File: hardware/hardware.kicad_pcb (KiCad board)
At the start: 2 copper layers, 33 x 44.4 mm, 18 parts, among them P1 PROG. UART, P2 WS2811, U1 MCP1754ST-3302E/MB, U2 74LS123, U3 SN74LV1T34

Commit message: Insert final timing component values and fix a missing trace in PCB.
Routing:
- net +3V3: track 66.3 -> 80.0 mm
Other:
- board text added: "SUBSPACE SIGN LED CONTROLLER R2 © 2016 MAKERS-IE"
- board text removed: "SUBSPACE SIGN LED CONTROLLER R1 © 2016 MAKERS-IE"
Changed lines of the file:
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@@
   (general
     (links 48)
-    (no_connects 1)
+    (no_connects 0)
     (area 69.992572 22.779999 132.445429 80.090001)
     (thickness 1.6)
     (drawings 11)
-    (tracks 176)
+    (tracks 179)
     (zones 0)
     (modules 18)
@@
     (32 B.Adhes user)
     (33 F.Adhes user)
-    (34 B.Paste user)
+    (34 B.Paste user hide)
     (35 F.Paste user)
-    (36 B.SilkS user hide)
+    (36 B.SilkS user)
     (37 F.SilkS user hide)
     (38 B.Mask user)
@@
   )
   (setup
-    (last_trace_width 0.5)
+    (last_trace_width 0.375)
     (user_trace_width 0.375)
     (trace_clearance 0.2)
@@
       (effects (font (size 1 1) (thickness 0.15)))
     )
-    (fp_text value "PROG. UART" (at -2.667 6.35 360) (layer F.SilkS)
+    (fp_text value "PROG. UART" (at 3.175 19.304 360) (layer F.SilkS)
       (effects (font (size 1 1) (thickness 0.15)))
     )
@@
   (gr_line (start 78.74 77.47) (end 127 77.47) (angle 90) (layer Eco1.User) (width 0.15))
   (gr_line (start 78.74 29.21) (end 78.74 77.47) (angle 90) (layer Eco1.User) (width 0.15))
-  (gr_text "SUBSPACE SIGN\nLED CONTROLLER R1\n© 2016 MAKERS-IE" (at 93.472 39.624) (layer B.SilkS)
+  (gr_text "SUBSPACE SIGN\nLED CONTROLLER R2\n© 2016 MAKERS-IE" (at 93.472 39.624) (layer B.SilkS)
     (effects (font (size 1.5 1.5) (thickness 0.3)) (justify mirror))
   )
@@
   (segment (start 83.82 46.228) (end 86.868 46.228) (width 0.5) (layer F.Cu) (net 2))
   (segment (start 81.788 44.196) (end 83.82 46.228) (width 0.5) (layer F.Cu) (net 2))
+  (segment (start 92.456 56.007) (end 93.853 57.404) (width 0.5) (layer F.Cu) (net 3))
+  (segment (start 104.394 57.404) (end 105.25 58.26) (width 0.5) (layer F.Cu) (net 3))
+  (segment (start 93.853 57.404) (end 104.394 57.404) (width 0.5) (layer F.Cu) (net 3))
   (segment (start 106.426 45.72) (end 107.25 46.544) (width 0.5) (layer F.Cu) (net 3))
   (segment (start 107.25 46.544) (end 107.25 47.844) (width 0.5) (layer F.Cu) (net 3))
@@
   (segment (start 105.25 62.86502) (end 105.25 59.944) (width 0.5) (layer F.Cu) (net 3) (status 30))
   (segment (start 107.25 47.844) (end 107.25 49.214) (width 0.5) (layer F.Cu) (net 3) (status 10))
+  (segment (start 105.25 56.896) (end 105.25 58.26) (width 0.5) (layer F.Cu) (net 3) (status 20))
+  (segment (start 105.25 51.214) (end 105.25 56.896) (width 0.5) (layer F.Cu) (net 3))
   (segment (start 107.25 49.214) (end 105.25 51.214) (width 0.5) (layer F.Cu) (net 3))
-  (segment (start 105.25 51.214) (end 105.25 56.896) (width 0.5) (layer F.Cu) (net 3))
-  (segment (start 105.25 56.896) (end 105.25 59.944) (width 0.5) (layer F.Cu) (net 3) (status 20))
+  (segment (start 105.25 58.26) (end 105.25 59.944) (width 0.5) (layer F.Cu) (net 3) (status 20))
   (segment (start 87.376 40.706) (end 88.031 41.361) (width 0.375) (layer F.Cu) (net 4))
   (segment (start 88.031 41.361) (end 90.014 41.361) (width 0.375) (layer F.Cu) (net 4))
@@
   (segment (start 99.06 43.18) (end 99.06 44.45) (width 0.375) (layer F.Cu) (net 17))
   (segment (start 97.241 41.361) (end 99.06 43.18) (width 0.375) (layer F.Cu) (net 17))
-  (segment (start 95.25 55.88) (end 95.25 56.896) (width 0.5) (layer F.Cu) (net 19))
-  (segment (start 95.25 56.896) (end 95.25 56.992) (width 0.5) (layer B.Cu) (net 19))
-  (via (at 95.25 56.896) (size 0.6) (drill 0.4) (layers F.Cu B.Cu) (net 19))
-  (segment (start 94.838 57.404) (end 95.25 56.992) (width 0.5) (layer B.Cu) (net 19))
-  (segment (start 94.838 61.976) (end 94.838 57.404) (width 0.5) (layer B.Cu) (net 19) (status 10))
+  (segment (start 95.25 47.844) (end 95.25 56.388) (width 0.5) (layer F.Cu) (net 19))
+  (segment (start 94.838 56.8) (end 94.838 61.976) (width 0.5) (layer B.Cu) (net 19))
+  (segment (start 94.996 56.642) (end 94.838 56.8) (width 0.5) (layer B.Cu) (net 19))
+  (via (at 94.996 56.642) (size 0.6) (drill 0.4) (layers F.Cu B.Cu) (net 19))
+  (segment (start 95.25 56.388) (end 94.996 56.642) (width 0.5) (layer F.Cu) (net 19))
   (segment (start 105.41 69.215) (end 105.41 66.675) (width 0.5) (layer F.Cu) (net 19) (status 10))
   (segment (start 105.41 66.675) (end 104.013 65.278) (width 0.5) (layer F.Cu) (net 19))
-  (segment (start 95.25 55.88) (end 95.25 47.844) (width 0.5) (layer F.Cu) (net 19) (status 20))
   (segment (start 94.838 64.612) (end 94.838 61.976) (width 0.5) (layer B.Cu) (net 19) (status 20))
   (segment (start 94.996 64.77) (end 94.838 64.612) (width 0.5) (layer B.Cu) (net 19))

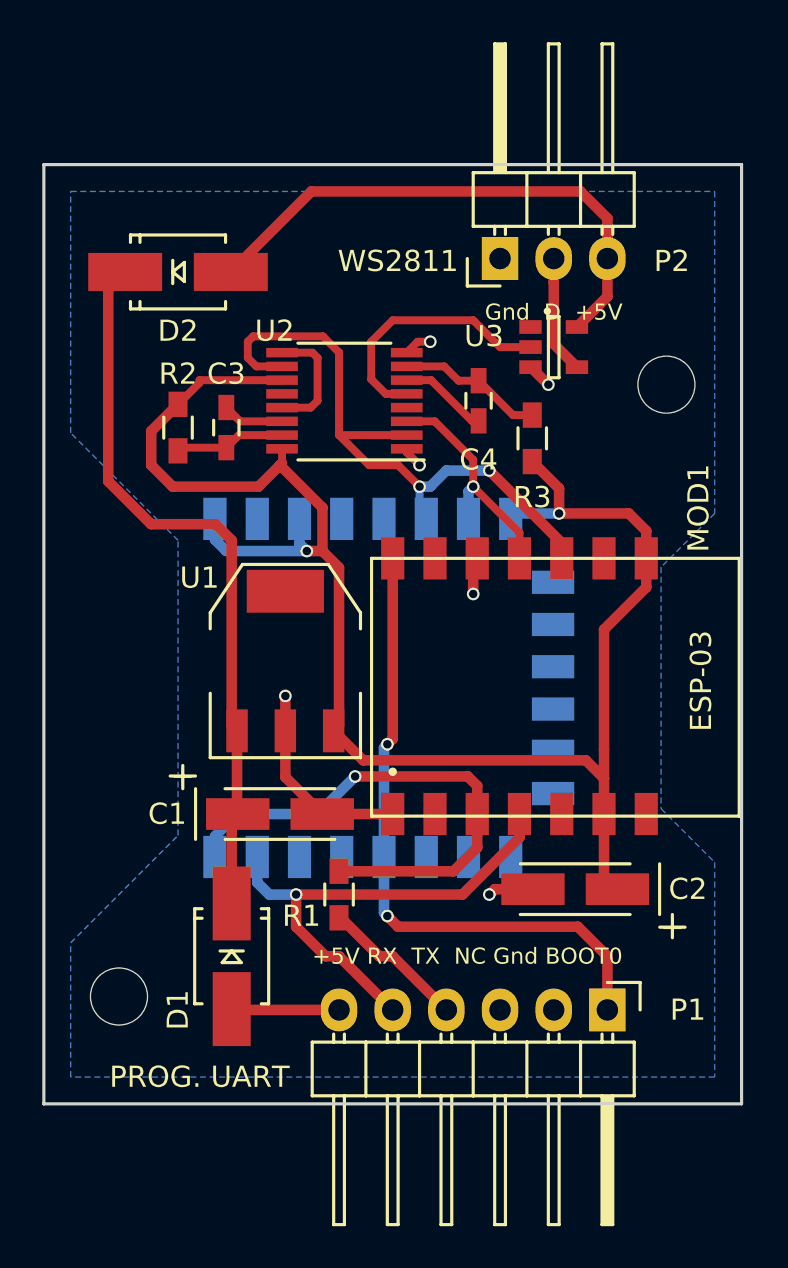
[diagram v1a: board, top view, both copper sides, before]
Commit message: Update firmware and hardware to use I2S.
No need for the multivibrators.
Need resistor to avoid short with UART TX.
Added resistor for easier bridging of U3.
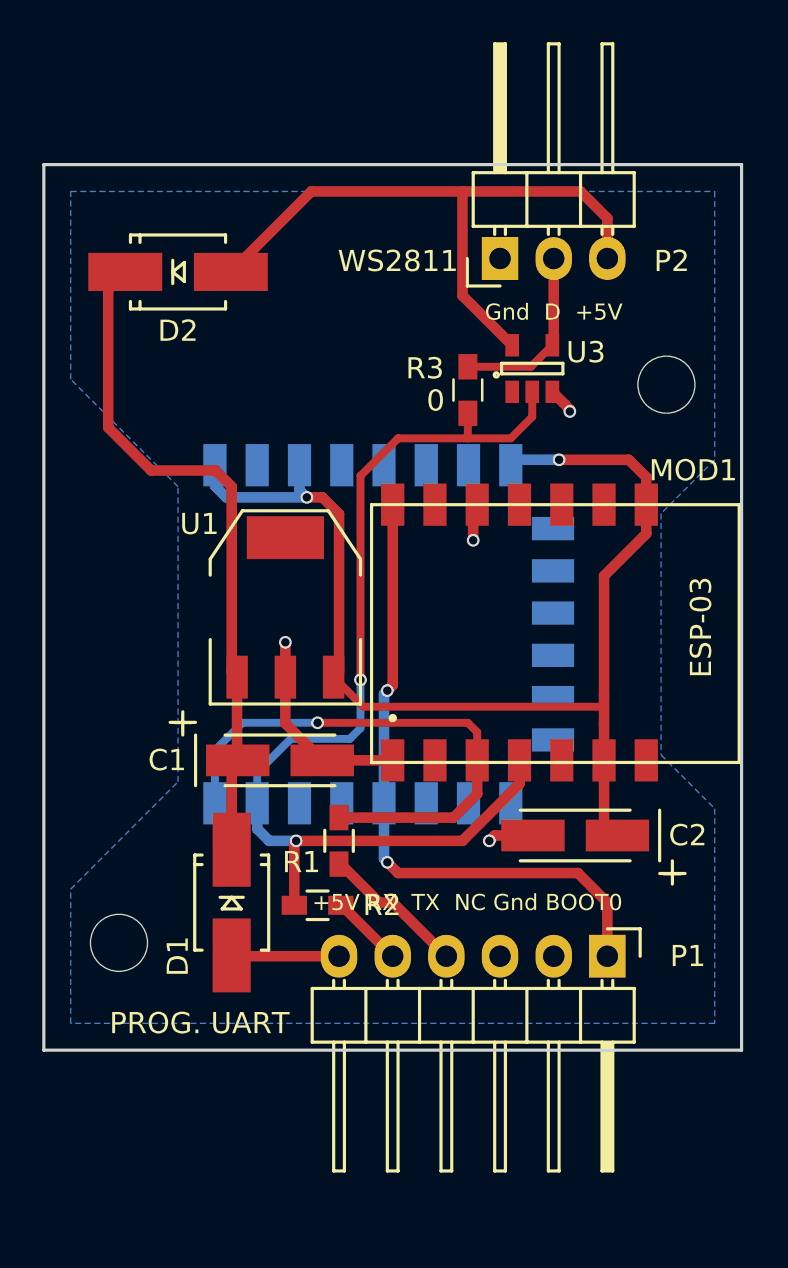
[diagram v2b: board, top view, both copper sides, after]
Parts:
- removed C3, C4: 300p, Capacitors_SMD:C_0603_HandSoldering
- removed U2: 74LS123, Housings_SSOP:TSSOP-16_4.4x5mm_Pitch0.65mm
- R2: value 1k -> 100
- R3: value 1k -> 0
- moved R2 23.6 mm to (91.7, 64.3), turned to 0 degrees
- moved R3 3.81 mm to (98.8, 39.9)
- moved P1 2.54 mm to (105.4, 66.7)
- moved C1 2.54 mm to (89.9, 57.4)
- moved C2 2.54 mm to (103.9, 61.0)
- moved MOD1 2.54 mm to (95.2, 57.4)
- moved MOD2 2.54 mm to (100.8, 59.4)
- moved R1 2.54 mm to (92.7, 61.2)
- moved U1 2.54 mm to (90.2, 50.2)
- moved D1 2.54 mm to (87.6, 64.1)
- moved REF** 2.54 mm to (82.3, 66.0)
- moved U3 1.44 mm to (101.9, 38.9), turned to 90 degrees
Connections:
- MOD1 pad 10: Net-(MOD1-Pad10) -> (no net)
- MOD1 pad 11: Net-(MOD1-Pad11) -> (no net)
- MOD1 pad 13: Net-(MOD1-Pad13) -> (no net)
- MOD1 pad 2: Net-(MOD1-Pad2) -> (no net)
- MOD1 pad 5: Net-(MOD1-Pad5) -> (no net)
- MOD1 pad 7: Net-(MOD1-Pad7) -> (no net)
- MOD1 pad 9: Net-(MOD1-Pad9) -> (no net)
- MOD2 pad 10: Net-(MOD2-Pad10) -> (no net)
- MOD2 pad 12: Net-(MOD2-Pad12) -> (no net)
- MOD2 pad 13: Net-(MOD2-Pad13) -> (no net)
- MOD2 pad 14: Net-(MOD1-Pad10) -> (no net)
- MOD2 pad 15: Net-(MOD1-Pad11) -> (no net)
- MOD2 pad 17: Net-(MOD2-Pad17) -> (no net)
- MOD2 pad 18: Net-(MOD2-Pad18) -> (no net)
- MOD2 pad 19: Net-(MOD2-Pad19) -> (no net)
- MOD2 pad 20: Net-(MOD2-Pad20) -> (no net)
- MOD2 pad 21: Net-(MOD2-Pad21) -> (no net)
- MOD2 pad 22: Net-(MOD2-Pad22) -> (no net)
- MOD2 pad 3: Net-(MOD2-Pad3) -> (no net)
- MOD2 pad 5: Net-(MOD2-Pad5) -> (no net)
- MOD2 pad 6: Net-(MOD2-Pad6) -> (no net)
- P1 pad 3: Net-(P1-Pad3) -> (no net)
- P1 pad 5: Net-(MOD1-Pad4) -> Net-(P1-Pad5)
- R2 pad 1: Net-(C3-Pad2) -> Net-(MOD1-Pad4)
- R2 pad 2: +3V3 -> Net-(P1-Pad5)
- R3 pad 1: Net-(C4-Pad2) -> Net-(P2-Pad2)
- R3 pad 2: +3V3 -> Net-(MOD1-Pad4)
- U3 pad 2: Net-(U2-Pad5) -> Net-(MOD1-Pad4)
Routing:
- net Net-(MOD1-Pad10): track 30.8 -> 0.00 mm, vias 2 -> 0
- net Net-(MOD1-Pad4): track 23.8 -> 50.0 mm, vias 1 -> 2
- net +3V3: track 80.0 -> 55.2 mm
- net Net-(U2-Pad5): track 12.2 -> 0.00 mm
- net Net-(MOD1-Pad11): track 11.1 -> 0.00 mm, vias 1 -> 0
- net Net-(C4-Pad2): track 6.89 -> 0.00 mm
- net Net-(U2-Pad13): track 5.63 -> 0.00 mm
- net Net-(C3-Pad2): track 5.23 -> 0.00 mm
- net Net-(D2-Pad2): track 26.3 -> 30.7 mm
- net Net-(C4-Pad1): track 4.20 -> 0.00 mm
- net Net-(P1-Pad5): track 0.00 -> 3.59 mm
- net Net-(C3-Pad1): track 2.91 -> 0.00 mm
- net Net-(P2-Pad2): track 6.23 -> 8.55 mm
- net GND: track 17.1 -> 14.9 mm, vias 6 -> 4
- net +5V: track 35.1 -> 33.7 mm
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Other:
- board size 33 x 44.4 mm -> 33 x 41.9 mm
- board text added: "SUBSPACE SIGN LED CONTROLLER R3 © 2016 MAKERS-IE"
- board text removed: "SUBSPACE SIGN LED CONTROLLER R2 © 2016 MAKERS-IE"
